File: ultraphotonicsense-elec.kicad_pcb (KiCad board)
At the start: 2 copper layers, 88 x 38 mm, 77 parts, among them J1 Conn_SWD_UART, J10 Conn_01x04, J11 Conn_01x04, J12 Conn_01x04, J13 Conn_01x04, J2 Conn_01x05, J3 Conn_01x05, J4 Conn_01x05, J5 Conn_01x05, J6 Conn_01x05, J7 Conn_01x05, J8 Conn_01x05, J9 Conn_01x05, P1 CAN_conn, P2 CAN_conn, Q1 BSS138, Q2 BSS138, Q3 BSS138, Q4 BSS138, Q5 BSS138, U1 TXB0108PW, U2 74HC164, U3 MCP2551-I-SN, U4 LD1117S50TR_SOT223, U5 LD1117S33TR_SOT223, U6 LP38693MP-ADJ, U7 STM32F303K8Tx, Y1 Crystal

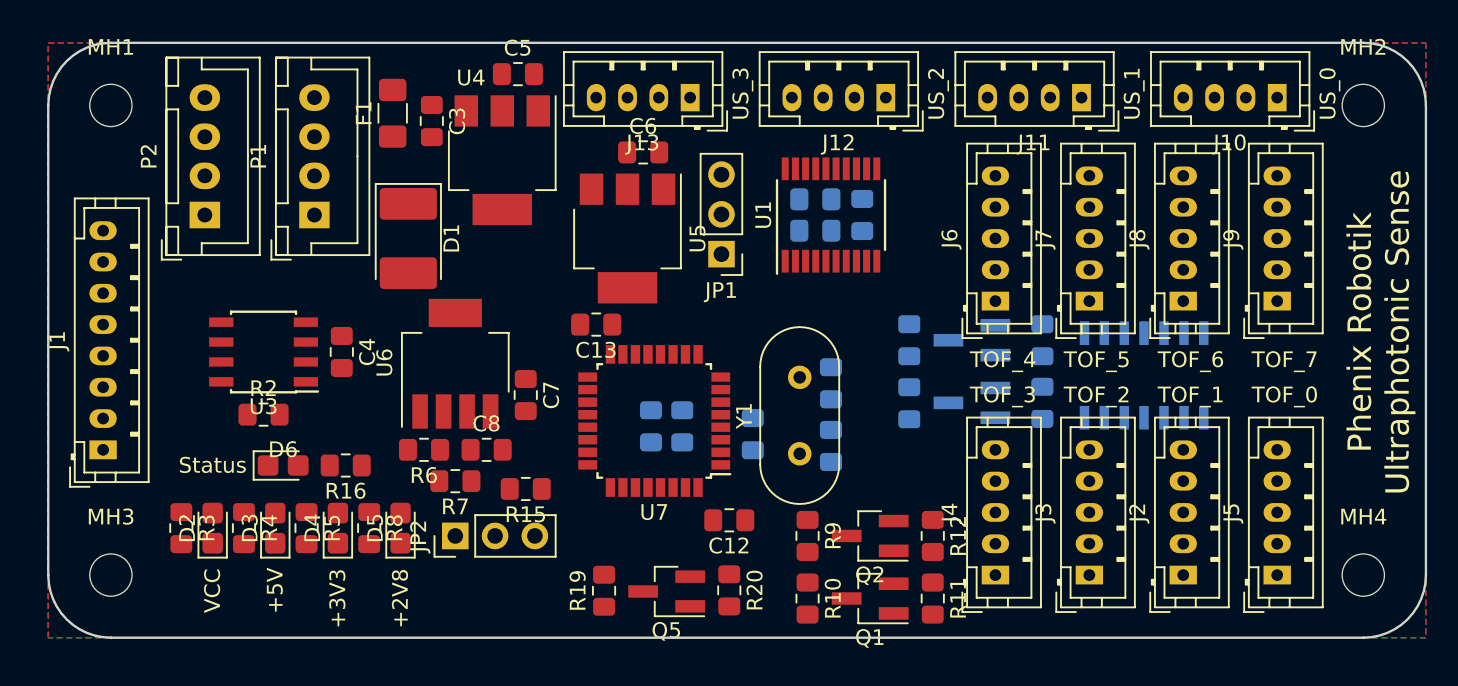
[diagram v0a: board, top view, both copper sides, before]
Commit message: PCB routed, no errors but still a few tracks too close
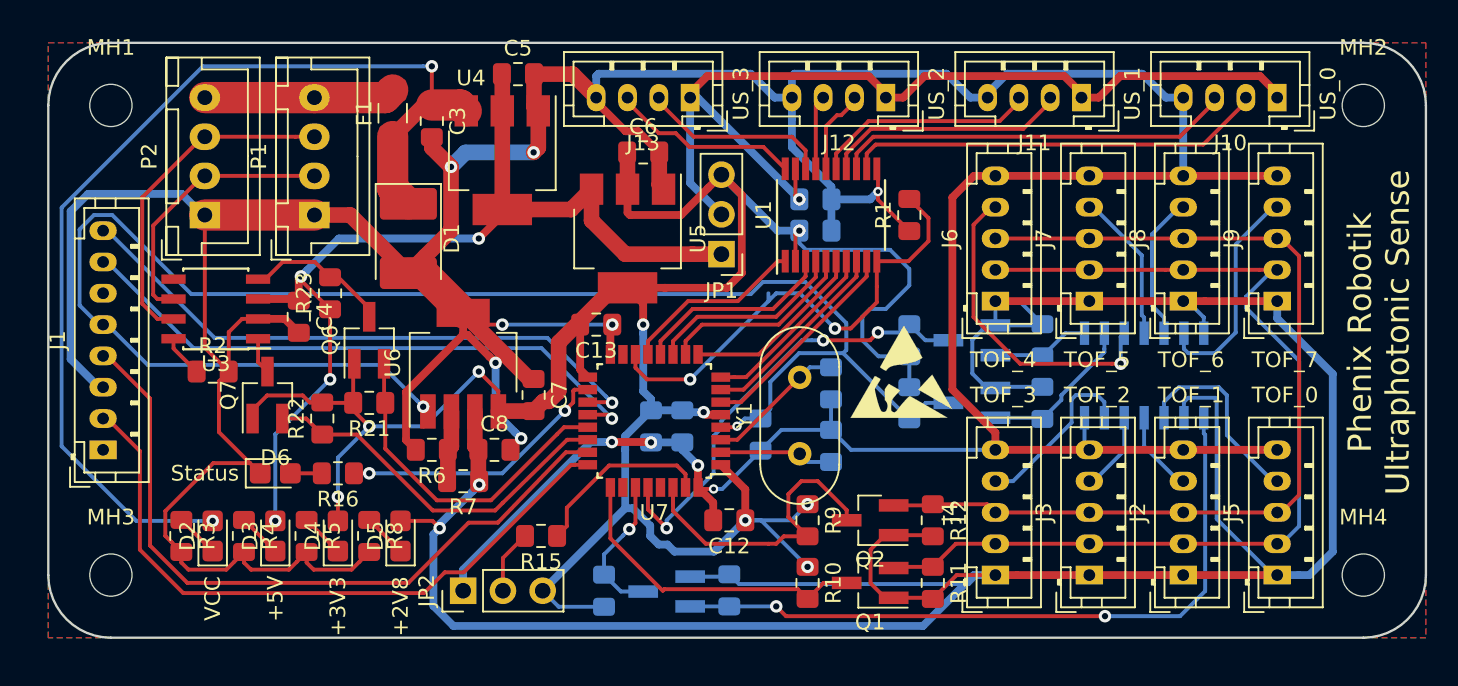
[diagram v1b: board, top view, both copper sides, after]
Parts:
- added Q6: BSS138, Package_TO_SOT_SMD:SOT-23_Handsoldering, F.Cu at (56.5, 55.0)
- added Q7: BSS138, Package_TO_SOT_SMD:SOT-23_Handsoldering, F.Cu at (50.0, 58.5)
- added R21: R, Resistor_SMD:R_0805_2012Metric_Pad1.15x1.40mm_HandSolder, F.Cu at (56.5, 59.0)
- added R22: R, Resistor_SMD:R_0805_2012Metric_Pad1.15x1.40mm_HandSolder, F.Cu at (53.5, 60.0)
- added R23: R, Resistor_SMD:R_0805_2012Metric_Pad1.15x1.40mm_HandSolder, F.Cu at (54.0, 52.0)
- added REF**: KiCad-Logo2_6mm_SilkScreen, Symbol:KiCad-Logo2_6mm_SilkScreen, B.Cu at (87.0, 67.0)
- added REF**: ESD-Logo_6.6x6mm_SilkScreen, Symbol:ESD-Logo_6.6x6mm_SilkScreen, F.Cu at (90.5, 57.0)
- added REF**: OSHW-Logo2_7.3x6mm_SilkScreen, Symbol:OSHW-Logo2_7.3x6mm_SilkScreen, B.Cu at (74.5, 67.5)
- Q5, R19, R20: moved to B.Cu
- R1: moved to F.Cu
- moved R2 4.26 mm to (46.5, 57.0)
- moved U3 4.11 mm to (46.7, 53.0)
- moved C4 3.55 mm to (52.0, 53.5)
- moved JP2 3.54 mm to (62.5, 71.0)
- moved R15 3.15 mm to (67.5, 67.5)
- moved R1 3.00 mm to (91.0, 47.0), turned to 90 degrees
- moved Q1 1.00 mm to (88.5, 70.5)
- moved Q2 1.00 mm to (88.5, 66.5)
- moved R10 1.00 mm to (84.5, 70.5)
- moved R11 1.00 mm to (92.5, 70.5)
- moved R12 1.00 mm to (92.5, 66.5)
- moved R9 1.00 mm to (84.5, 66.5)
- moved D6 0.71 mm to (50.5, 63.5)
- moved R16 0.71 mm to (54.5, 63.5)
- moved C11 0.50 mm to (81.5, 61.0)
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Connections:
- J1 pad 1: +3V3 -> Net-(J1-Pad1)
- U3 pad 1: /STM32F303K8/CAN_TX -> Net-(Q7-Pad3)
- U3 pad 4: /STM32F303K8/CAN_RX -> Net-(Q6-Pad3)
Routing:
- net GND: track 0.00 -> 336.6 mm, vias 0 -> 11
- net +2V8: track 0.00 -> 183.6 mm, vias 0 -> 2
- net +3V3: track 0.00 -> 161.2 mm, vias 0 -> 9
- net /Power_CAN/2V8_EN: track 0.00 -> 104.0 mm, vias 0 -> 2
- net Net-(C3-Pad1): track 0.00 -> 69.0 mm, vias 0 -> 2
- net ToF_SCL: track 0.00 -> 63.8 mm
- net +5V: track 0.00 -> 63.0 mm, vias 0 -> 4
- net ToF_SDA: track 0.00 -> 61.7 mm
- net US_PWR: track 0.00 -> 61.6 mm, vias 0 -> 1
- net /STM32F303K8/SWDIO: track 0.00 -> 46.0 mm
- net /Level_Conv_0/OUT_2V8: track 0.00 -> 44.9 mm, vias 0 -> 2
- net /STM32F303K8/SWCLK: track 0.00 -> 42.7 mm
- net /STM32F303K8/UART_TX: track 0.00 -> 38.6 mm, vias 0 -> 1
- net /STM32F303K8/UART_RX: track 0.00 -> 38.3 mm, vias 0 -> 1
- net /STM32F303K8/US_OE: track 0.00 -> 30.5 mm, vias 0 -> 2
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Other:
- net class Alim_3V added: clearance 0.4, trace_width 0.5, via_dia 0.8, via_drill 0.4
- rule pad_to_mask_clearance: 0.2 -> 0.4

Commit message: Improved tracks spacing
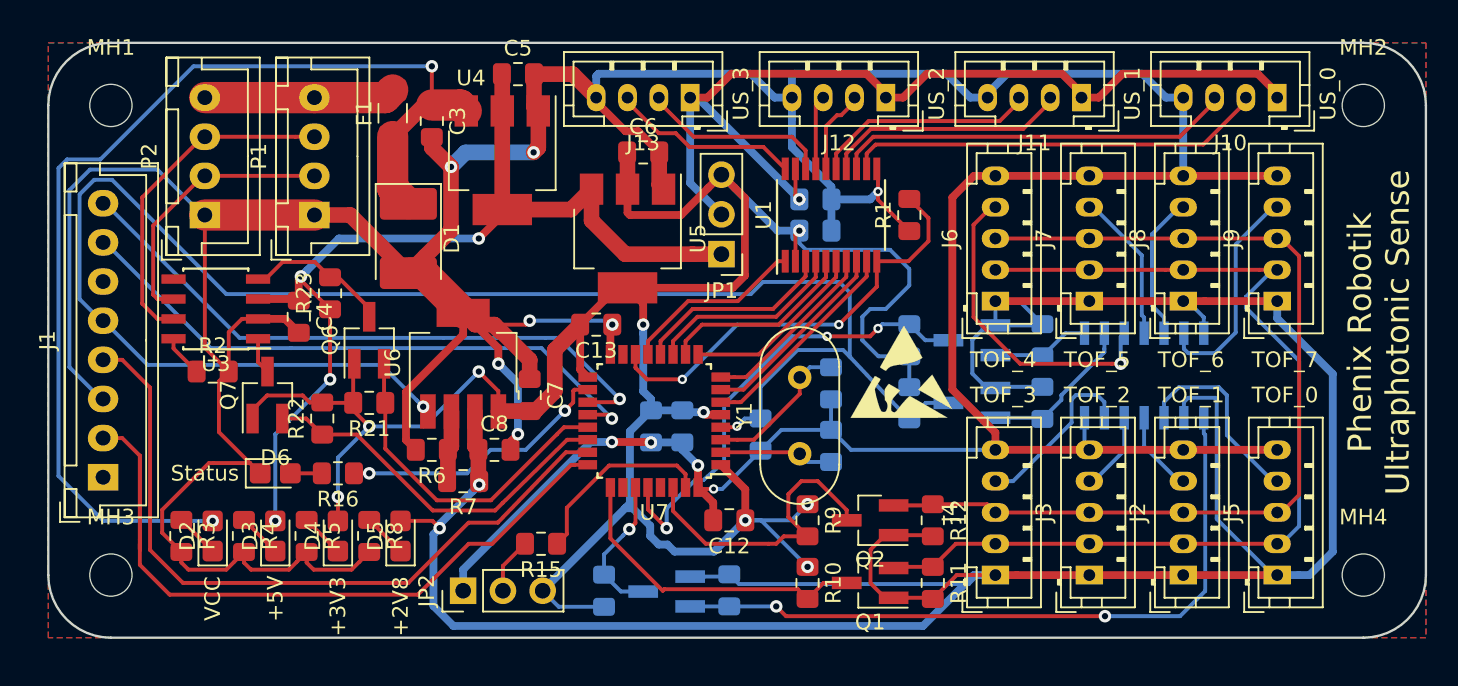
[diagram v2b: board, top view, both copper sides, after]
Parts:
- J1: footprint Connector_JST:JST_PH_B8B-PH-K_1x08_P2.00mm_Vertical -> Connector_JST:JST_XH_B08B-XH-A_1x08_P2.50mm_Vertical
- moved J1 1.75 mm to (39.5, 63.8)
- moved REF** 1.03 mm to (74.8, 66.5)
- moved REF** 1.00 mm to (87.0, 66.0)
- moved R15 0.50 mm to (67.5, 68.0)
- moved C7 0.25 mm to (66.8, 58.5)
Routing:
- net /STM32F303K8/SWCLK: track 42.7 -> 49.0 mm
- net GND: track 336.6 -> 342.1 mm
- net /Power_CAN/2V8_EN: track 104.0 -> 108.8 mm
- net +3V3: track 161.2 -> 157.3 mm
- net Net-(C3-Pad1): track 69.0 -> 72.0 mm
- net /STM32F303K8/US_OE: track 30.5 -> 27.6 mm
- net /STM32F303K8/UART_TX: track 38.6 -> 40.3 mm
- net /Level_Conv_1/IN_3V3: track 28.9 -> 29.8 mm
- net Net-(C10-Pad1): track 8.96 -> 9.58 mm
- net /STM32F303K8/UART_RX: track 38.3 -> 38.8 mm
- net Net-(JP2-Pad2): track 4.08 -> 3.58 mm

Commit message: Corrected, routing redone
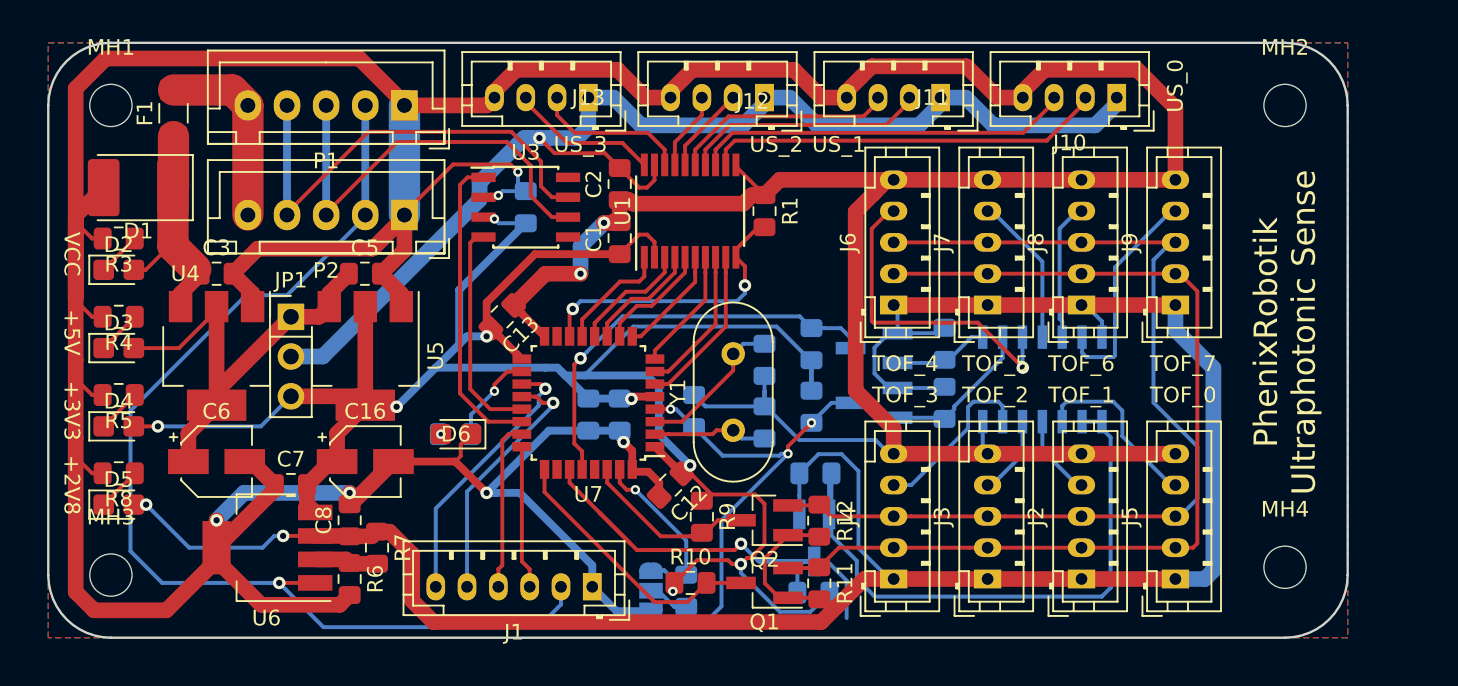
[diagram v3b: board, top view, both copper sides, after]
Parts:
- removed Q6, Q7: BSS138, Package_TO_SOT_SMD:SOT-23_Handsoldering
- removed R2: 47kR, Resistor_SMD:R_0805_2012Metric_Pad1.15x1.40mm_HandSolder
- removed R21, R22, R23: R, Resistor_SMD:R_0805_2012Metric_Pad1.15x1.40mm_HandSolder
- removed REF**: Logo_25,4mm, PhoenixRobotik:Logo_25,4mm
- removed REF**: KiCad-Logo2_6mm_SilkScreen, Symbol:KiCad-Logo2_6mm_SilkScreen
- removed REF**: ESD-Logo_6.6x6mm_SilkScreen, Symbol:ESD-Logo_6.6x6mm_SilkScreen
- removed REF**: OSHW-Logo2_7.3x6mm_SilkScreen, Symbol:OSHW-Logo2_7.3x6mm_SilkScreen
- added C16: 10µ, Capacitor_SMD:CP_Elec_4x5.4, F.Cu at (56.2, 62.8)
- C1, C2: moved to F.Cu
- C3, C5: value C -> 100n
- C4, R15, R16: moved to B.Cu
- C6: value C -> 10µ; footprint Capacitor_SMD:C_0805_2012Metric_Pad1.15x1.40mm_HandSolder -> Capacitor_SMD:CP_Elec_4x5.4
- C7, C8: value C -> 1µ
- J1: value Conn_SWD_UART -> Conn_Debug; footprint Connector_JST:JST_XH_B08B-XH-A_1x08_P2.50mm_Vertical -> Connector_JST:JST_PH_B6B-PH-K_1x06_P2.00mm_Vertical
- JP2: footprint Connector_PinHeader_2.54mm:PinHeader_1x03_P2.54mm_Vertical -> Jumper:SolderJumper-3_P1.3mm_Open_RoundedPad1.0x1.5mm; moved to B.Cu
- P1, P2: footprint Connector_JST:JST_XH_B04B-XH-A_1x04_P2.50mm_Vertical -> Connector_JST:JST_XH_B05B-XH-A_1x05_P2.50mm_Vertical
- U3: value MCP2551-I-SN -> TCAN332
- Y1: footprint Crystal:Crystal_HC49-U_Vertical -> Crystal:Crystal_HC49-4H_Vertical
- moved C6 33.7 mm to (46.8, 62.8)
- moved J1 32.0 mm to (70.8, 70.8), turned to 180 degrees
- moved JP1 27.8 mm to (51.5, 53.5), turned to 0 degrees
- moved U4 22.1 mm to (46.8, 56.0)
- moved U3 20.8 mm to (66.5, 46.5), turned to 0 degrees
- moved R3 19.4 mm to (40.5, 48.5), turned to 180 degrees
- moved U5 18.4 mm to (56.2, 56.0)
- moved D5 18.1 mm to (40.5, 65.5), turned to 0 degrees
- moved D2 18.0 mm to (40.5, 50.5), turned to 0 degrees
- moved D1 17.6 mm to (41.8, 45.2), turned to 180 degrees
- moved U6 17.2 mm to (50.0, 68.2), turned to 180 degrees
- moved C3 16.9 mm to (46.8, 50.8), turned to 0 degrees
- moved R8 16.5 mm to (40.5, 63.5), turned to 180 degrees
- moved C7 16.3 mm to (51.5, 64.2), turned to 0 degrees
- moved R4 16.1 mm to (40.5, 53.5), turned to 180 degrees
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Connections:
- C11 pad 2: /Power_CAN/2V8_EN -> /Level_Conv_2/IN_3V3
- C4 pad 1: +5V -> +3V3
- C6 pad 1: +3V3 -> +5V
- J1 pad 1: Net-(J1-Pad1) -> GND
- J1 pad 2: /STM32F303K8/SWCLK -> /Level_Conv_2/IN_3V3
- J1 pad 3: GND -> /STM32F303K8/SWCLK
- J1 pad 5: /Power_CAN/2V8_EN -> /STM32F303K8/UART_RX
- J1 pad 6: Net-(J1-Pad6) -> /STM32F303K8/UART_TX
- P1 pad 2: Net-(P1-Pad2) -> /Level_Conv_2/IN_3V3
- P1 pad 4: /Power_CAN/+7V_CAN -> Net-(P1-Pad4)
- P2 pad 2: Net-(P1-Pad2) -> /Level_Conv_2/IN_3V3
- P2 pad 4: /Power_CAN/+7V_CAN -> Net-(P1-Pad4)
- Q3 pad 3: /Power_CAN/2V8_EN -> /Level_Conv_2/IN_3V3
- R13 pad 1: /Power_CAN/2V8_EN -> /Level_Conv_2/IN_3V3
- U2 pad 2: +2V8 -> /Level_Conv_0/OUT_2V8
- U3 pad 1: Net-(Q7-Pad3) -> /STM32F303K8/CAN_TX
- U3 pad 3: +5V -> +3V3
- U3 pad 4: Net-(Q6-Pad3) -> /STM32F303K8/CAN_RX
- U3 pad 5: Net-(U3-Pad5) -> (no net)
- U3 pad 6: Net-(P1-Pad2) -> Net-(P1-Pad3)
- U3 pad 7: Net-(P1-Pad3) -> Net-(P1-Pad4)
- U3 pad 8: Net-(R2-Pad1) -> (no net)
- U6 pad 1: /Power_CAN/2V8_EN -> /Level_Conv_2/IN_3V3
- U7 pad 15: Net-(U7-Pad15) -> (no net)
- U7 pad 26: Net-(U7-Pad26) -> (no net)
- U7 pad 29: Net-(U7-Pad29) -> (no net)
- U7 pad 4: /Power_CAN/2V8_EN -> /Level_Conv_2/IN_3V3
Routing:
- net /Level_Conv_2/IN_3V3: track 0.00 -> 111.5 mm, vias 0 -> 4
- net /Power_CAN/2V8_EN: track 108.8 -> 0.00 mm, vias 2 -> 0
- net Net-(C3-Pad1): track 72.0 -> 14.8 mm, vias 2 -> 0
- net /STM32F303K8/SWCLK: track 49.0 -> 9.13 mm
- net /STM32F303K8/SWDIO: track 46.4 -> 10.9 mm
- net GND: track 342.1 -> 376.2 mm, vias 11 -> 8
- net +5V: track 63.0 -> 30.1 mm, vias 4 -> 0
- net Net-(P1-Pad4): track 0.00 -> 29.9 mm
- net +2V8: track 183.6 -> 154.2 mm
- net /Level_Conv_0/IN_3V3: track 9.35 -> 33.5 mm
- net /STM32F303K8/UART_TX: track 40.3 -> 17.2 mm
- net /STM32F303K8/UART_RX: track 38.8 -> 16.2 mm
- net Net-(P1-Pad2): track 17.4 -> 0.00 mm
- net US_PWR: track 61.8 -> 76.3 mm
- net Net-(R16-Pad1): track 17.6 -> 5.89 mm, vias 2 -> 1
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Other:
- board size 88 x 38 mm -> 83 x 38 mm
- board text added: "PhenixRobotik Ultraphotonic Sense"
- board text removed: "Phenix Robotik Ultraphotonic Sense"
- board text removed: "Status"

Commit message: Improved a few tracks
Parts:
- added REF**: Logo_16,9mm, PhoenixRobotik:Logo_16,9mm, B.Cu at (79.0, 50.0)
- added REF**: KiCad-Logo2_6mm_SilkScreen, Symbol:KiCad-Logo2_6mm_SilkScreen, B.Cu at (50.5, 66.5)
- added REF**: OSHW-Logo2_7.3x6mm_SilkScreen, Symbol:OSHW-Logo2_7.3x6mm_SilkScreen, B.Cu at (61.5, 67.0)
- moved R7 1.32 mm to (57.5, 69.5)
- moved R6 1.30 mm to (55.5, 71.5)
- moved U6 1.25 mm to (50.0, 69.5)
- moved C8 1.01 mm to (55.5, 67.5)
- moved R15 0.50 mm to (77.2, 71.0)
- moved R19 0.38 mm to (84.9, 71.5)
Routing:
- net +2V8: track 154.2 -> 167.1 mm
- net GND: track 376.2 -> 369.8 mm
- net /STM32F303K8/I2C_SDA: track 11.2 -> 14.2 mm
- net Net-(C9-Pad1): track 7.32 -> 9.44 mm
- net /Level_Conv_2/IN_3V3: track 111.5 -> 110.5 mm
- net +3V3: track 150.2 -> 151.2 mm
- net Net-(R15-Pad1): track 8.81 -> 9.36 mm
- net Net-(JP2-Pad2): track 2.67 -> 3.18 mm
